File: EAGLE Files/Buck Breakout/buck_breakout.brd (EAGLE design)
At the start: 100 x 80 mm, 14 parts

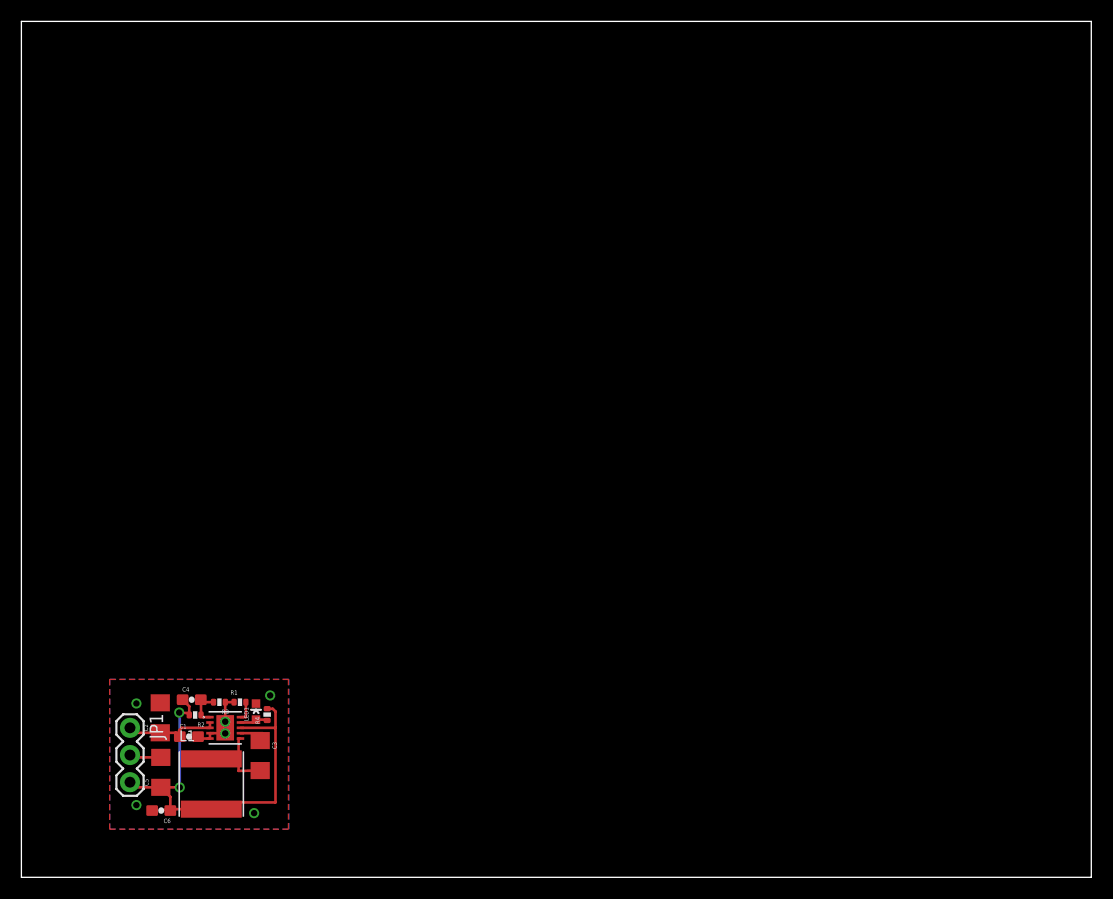
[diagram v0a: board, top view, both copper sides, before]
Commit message: Added polygons to power board. Text needs fixing.
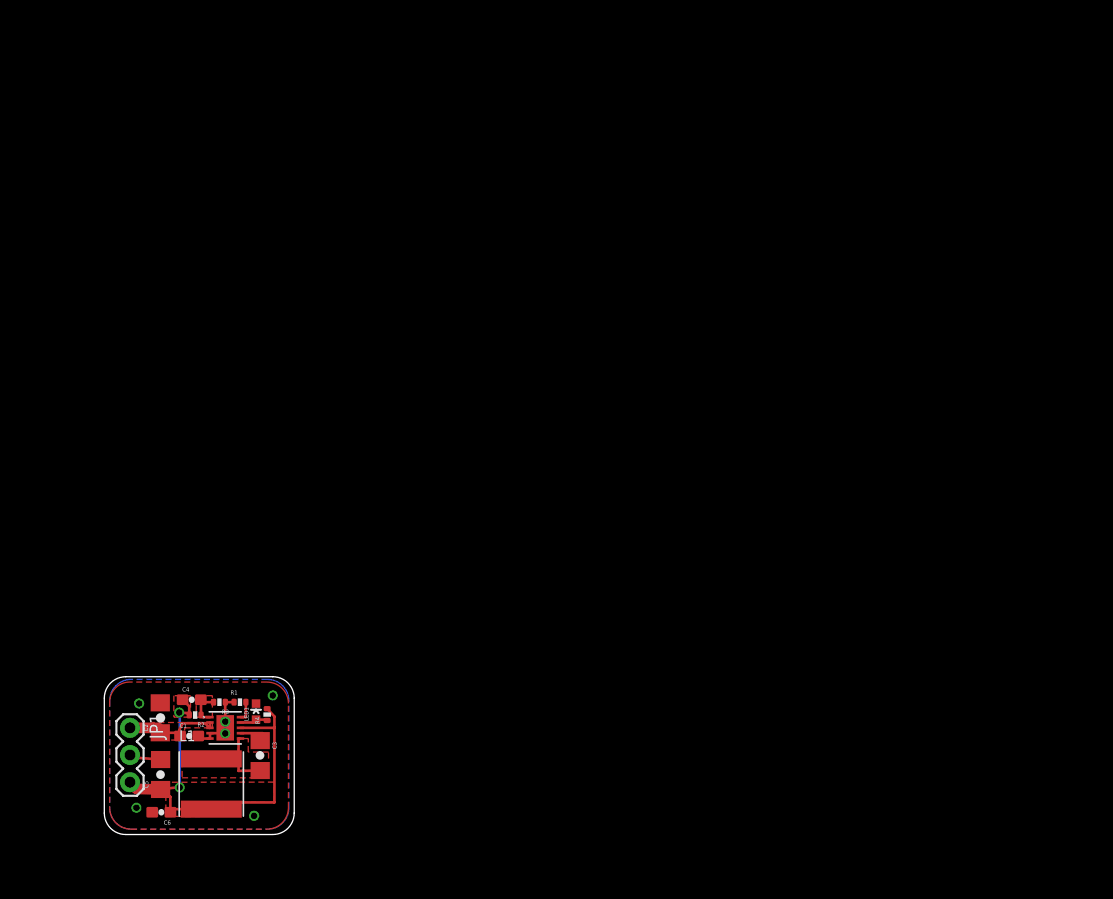
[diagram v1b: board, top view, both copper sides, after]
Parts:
- moved C5 0.20 mm to (13.0, 9.61)
- moved C6 0.16 mm to (13.1, 6.08)
- moved C1 0.06 mm to (15.7, 13.2)
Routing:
- net VOUT: track 40.9 -> 39.9 mm
- net VIN: track 9.09 -> 9.99 mm
- added copper zone on layer 1, net FB
- added copper zone on layer 1, net SW
- added copper zone on layer 1, net VIN
- added copper zone on layer 1, net VOUT
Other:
- board size 100 x 80 mm -> 17.8 x 14.8 mm

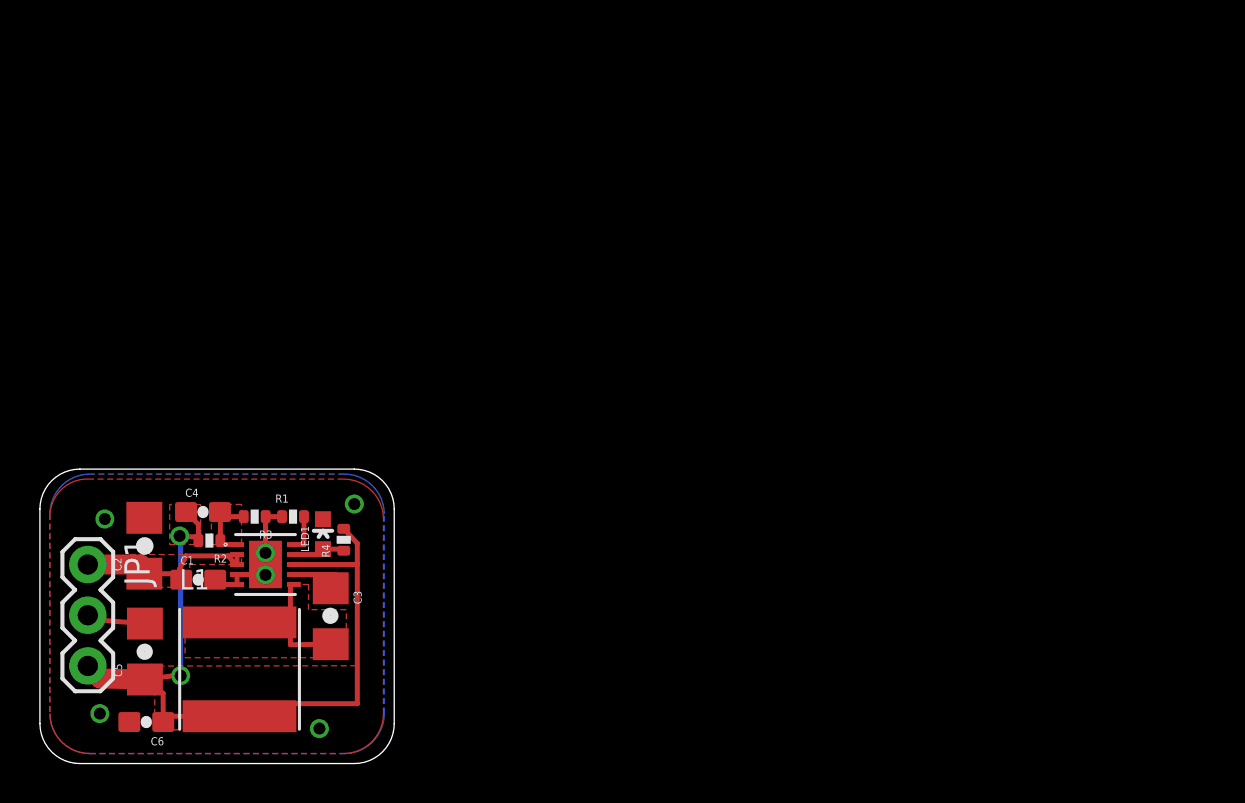
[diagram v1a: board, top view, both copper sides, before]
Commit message: Added linear reg to power board. Layout ver 1.
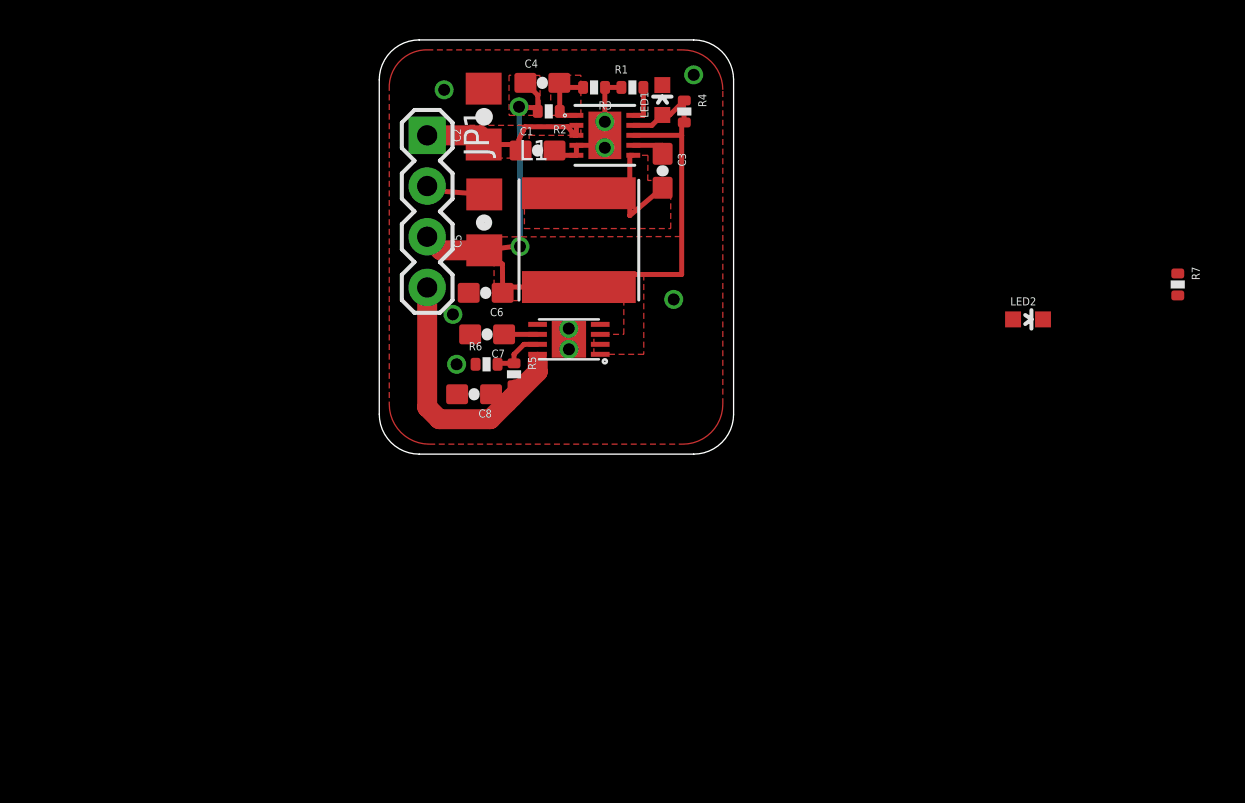
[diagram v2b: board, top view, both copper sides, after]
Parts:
- added C7: 1000pF, chips:0603-CAP
- added C8: 1uF, chips:0603-CAP
- added LED2: (no value), chips:LED-0603
- added R5, R6: 1M, chips:0402-S
- added R7: 330, chips:0402-S
- added U$2: MCP1725, intelliDesk:2X3_DFN
- C3: device chips:1206 -> chips:0603-CAP
- JP1: device SparkFun-Connectors:1X03 -> SparkFun-Connectors:1X04
- moved C3 27.8 mm to (38.9, 33.7)
- moved LED1 27.6 mm to (38.9, 37.2)
- moved R4 27.4 mm to (40.0, 36.7), turned to 270 degrees
- moved R2 27.4 mm to (33.2, 36.7)
- moved C1 27.4 mm to (32.7, 34.7)
- moved C2 27.4 mm to (30.0, 36.4)
- moved C4 27.4 mm to (32.9, 38.1)
- moved C5 27.4 mm to (30.0, 31.1)
- moved C6 27.4 mm to (30.1, 27.6)
- moved JP1 27.4 mm to (27.1, 35.5)
- moved L1 27.4 mm to (34.8, 30.2)
- moved R1 27.4 mm to (37.4, 37.9)
- moved U$1 27.4 mm to (36.0, 35.5)
- moved R3 27.4 mm to (35.5, 37.9)
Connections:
- removed net VOUT: C4.1, C5.1, C6.1, JP1.3, L1.2, R2.2, R4.2, U$1.8
- new net 3.3V: C8.1, JP1.4, R5.2, R7.1, U$2.8
- new net 3.6V: C4.1, C5.1, C6.1, JP1.3, L1.2, R2.2, R4.2, U$1.8, U$2.1, U$2.2, U$2.3
- new net N$1: LED2.A, R7.2, U$2.5
- new net N$5: C7.1, U$2.6
- new net N$6: R5.1, R6.2, U$2.7
- net GND: now also C7.2, C8.2, LED2.C, R6.1, U$2.4, U$2.EP
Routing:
- net VOUT: track 39.9 -> 0.00 mm, vias 2 -> 0
- net 3.6V: track 0.00 -> 37.3 mm, vias 0 -> 2
- net 3.3V: track 0.00 -> 15.3 mm
- net N$6: track 0.00 -> 2.68 mm
- net N$5: track 0.00 -> 1.68 mm
- net N$4: track 2.82 -> 1.90 mm
- net GND: vias 6 -> 9
- added copper zone on layer 1, net 3.6V
- removed copper zone on layer 16, net GND
- removed copper zone on layer 1, net VOUT
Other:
- board size 17.8 x 14.8 mm -> 17.8 x 20.8 mm

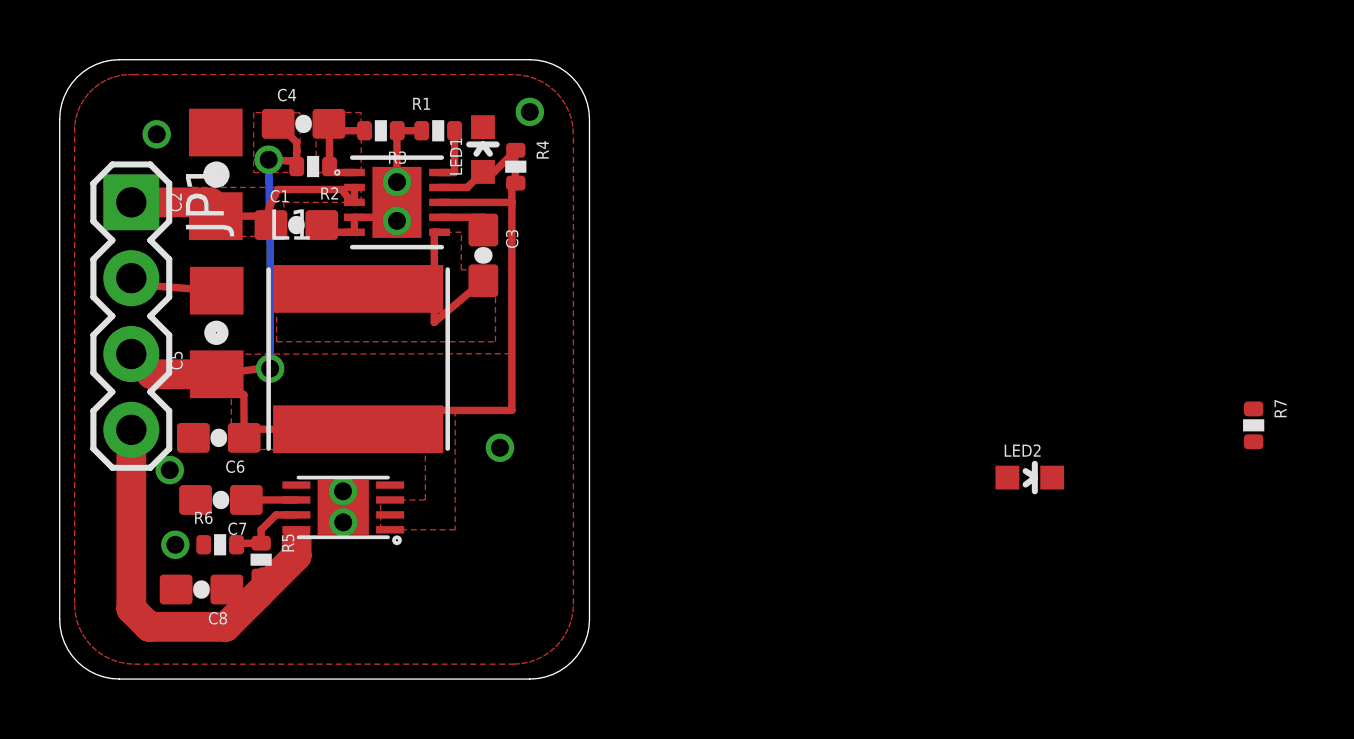
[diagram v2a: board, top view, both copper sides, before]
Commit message: Rerouted for nicer layout on linear supply
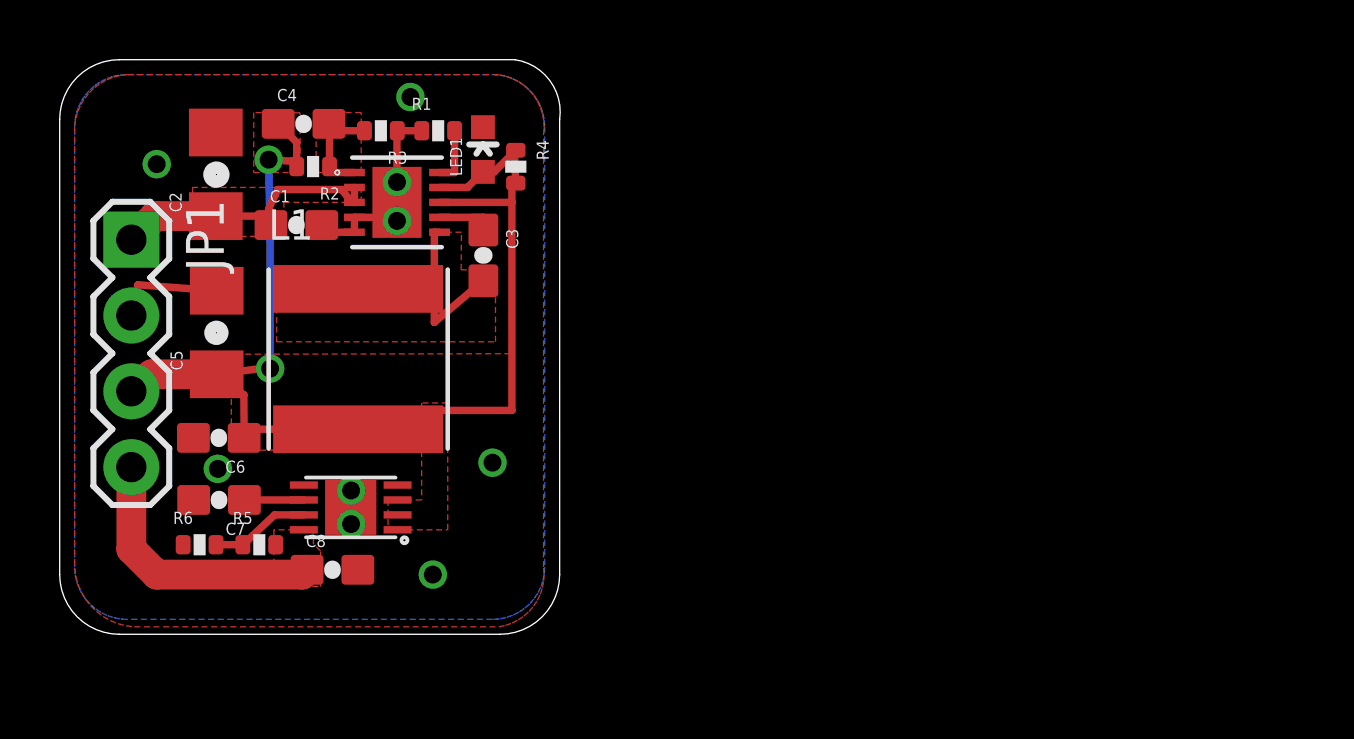
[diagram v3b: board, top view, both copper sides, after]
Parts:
- removed LED2: (no value), chips:LED-0603
- removed R7: 330, chips:0402-S
- moved C8 4.44 mm to (33.9, 23.2), turned to 0 degrees
- moved JP1 1.25 mm to (27.1, 34.2)
- moved R6 0.69 mm to (29.4, 24.0)
- moved R5 0.50 mm to (31.4, 24.0), turned to 0 degrees
- moved U$2 0.25 mm to (34.5, 25.2)
- moved C7 0.06 mm to (30.1, 25.5)
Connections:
- removed net N$1: LED2.A, R7.2, U$2.5
- net 3.3V: no longer R7.1
- net GND: no longer LED2.C
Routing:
- net 3.3V: track 15.3 -> 9.06 mm
- net GND: track 9.96 -> 10.7 mm
- net N$6: track 2.68 -> 3.34 mm
- added copper zone on layer 1, net 3.3V
- added copper zone on layer 16, net GND
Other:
- board size 17.8 x 20.8 mm -> 16.8 x 19.2 mm

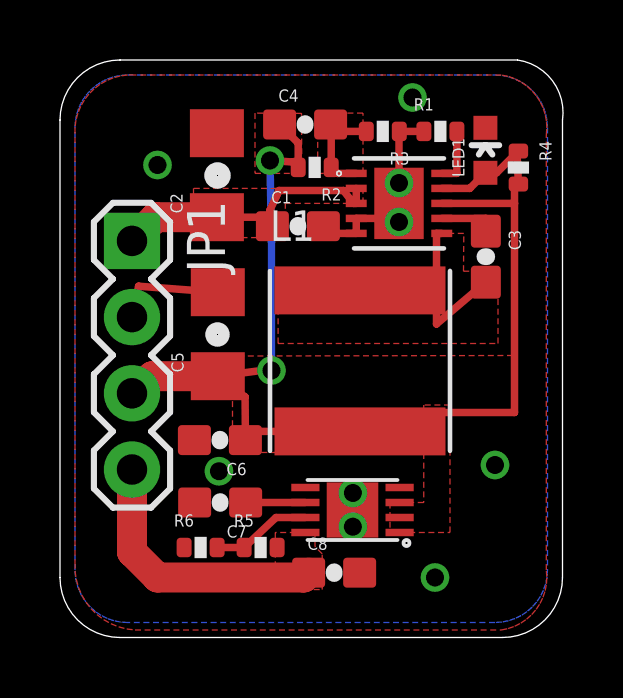
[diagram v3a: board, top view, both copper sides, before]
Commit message: fixed via size and removed most silkscreen on power breakout pcb
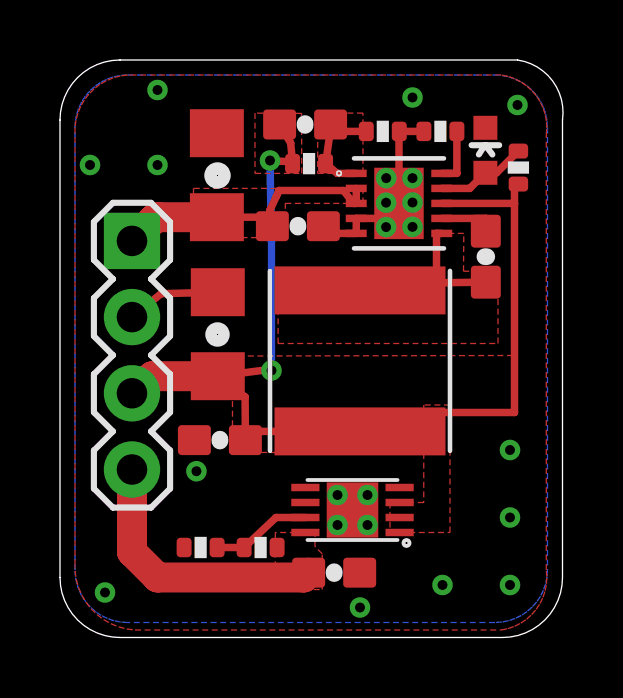
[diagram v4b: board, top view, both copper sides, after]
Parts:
- removed C7: 1000pF, chips:0603-CAP
- moved R2 0.23 mm to (33.1, 36.8)
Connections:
- removed net N$5: C7.1, U$2.6
- net GND: no longer C7.2
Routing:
- net N$5: track 1.99 -> 0.00 mm
- net SW: track 8.17 -> 6.41 mm
- net 3.6V: track 37.2 -> 35.6 mm
- net GND: track 10.7 -> 10.1 mm, vias 9 -> 22

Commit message: Removed unneeded capacitor on linear supply. Turns out that cap was needed only for power good indicator.
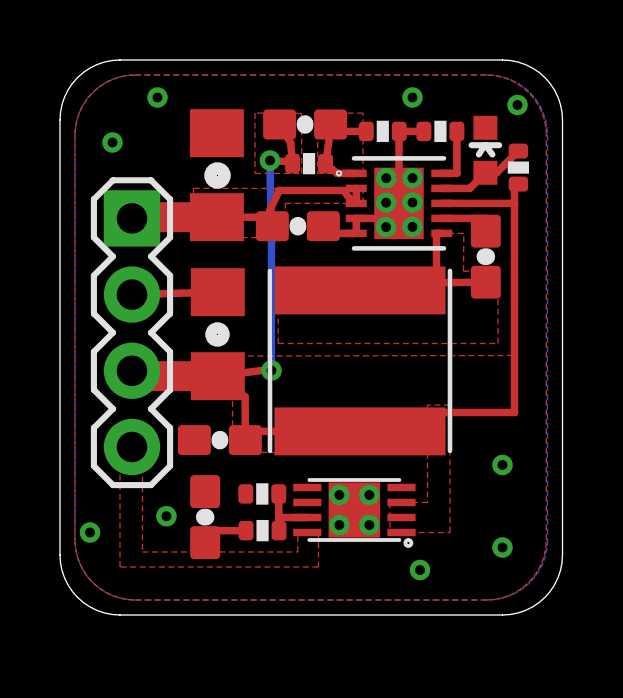
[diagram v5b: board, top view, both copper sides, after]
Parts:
- moved C8 4.68 mm to (29.6, 25.0), turned to 90 degrees
- moved R6 2.72 mm to (31.5, 25.8)
- moved JP1 0.75 mm to (27.1, 35.0)
- moved R5 0.57 mm to (31.5, 24.6), turned to 180 degrees
- moved U$2 0.06 mm to (34.6, 25.2)
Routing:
- net 3.3V: track 9.06 -> 1.76 mm
- net N$6: track 3.34 -> 2.17 mm
- net GND: track 10.1 -> 9.86 mm, vias 22 -> 19
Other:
- board size 16.8 x 19.2 mm -> 16.8 x 18.5 mm

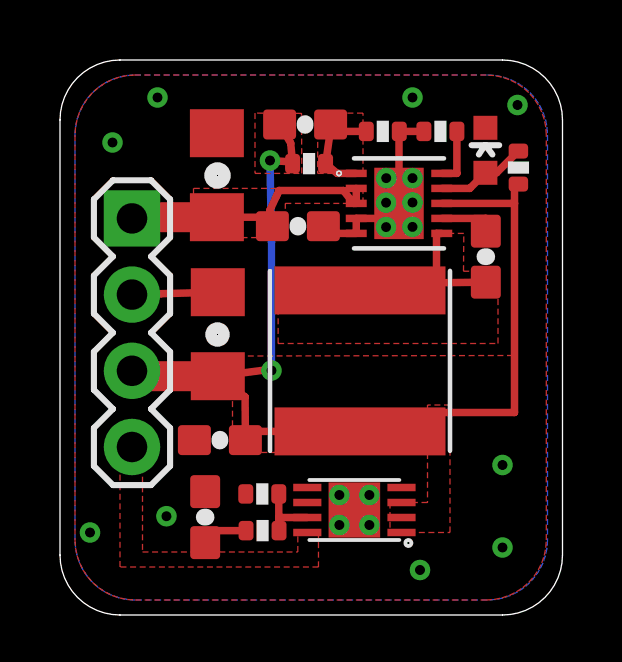
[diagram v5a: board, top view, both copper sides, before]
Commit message: Added OLED breakout board. (not yet designed) Added linear regulator datasheet. Updated parts library.
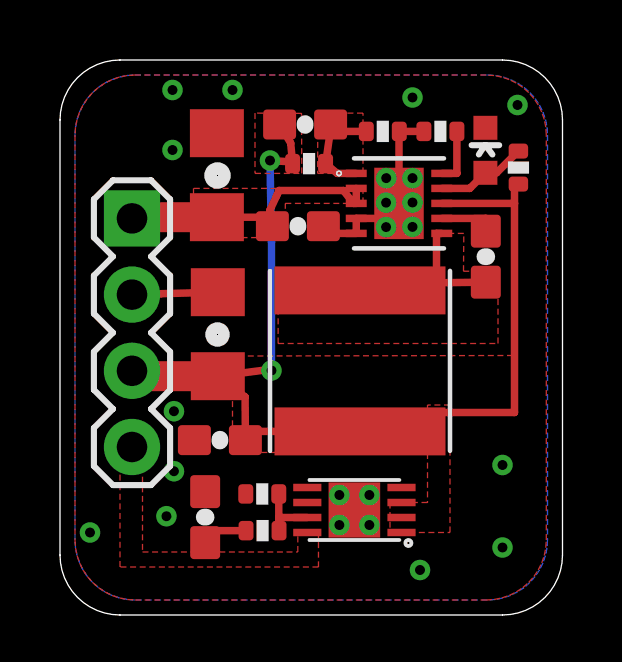
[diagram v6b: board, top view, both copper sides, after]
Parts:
- R5: value 1M -> 1.1M
- R6: value 1M -> 160k
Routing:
- net GND: vias 19 -> 22
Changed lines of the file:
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@@
 </element>
 <element name="U$2" library="intelliDesk" package="2X3_DFN" value="MCP1725" x="34.5626" y="25.25" smashed="yes" rot="R180"/>
-<element name="R5" library="chips" package="0402-S" value="1M" x="31.5016" y="24.5622" smashed="yes" rot="R180"/>
-<element name="R6" library="chips" package="0402-S" value="1M" x="31.4926" y="25.7852" smashed="yes"/>
+<element name="R5" library="chips" package="0402-S" value="1.1M" x="31.5016" y="24.5622" smashed="yes" rot="R180"/>
+<element name="R6" library="chips" package="0402-S" value="160k" x="31.4926" y="25.7852" smashed="yes"/>
 <element name="C8" library="chips" package="0603-CAP" value="1uF" x="29.5886" y="25.0124" smashed="yes" rot="R90"/>
 </elements>
@@
 <via x="36.5" y="35.5" extent="1-16" drill="0.3302"/>
 <via x="36.5" y="34.6874" extent="1-16" drill="0.3302"/>
-<via x="26.5" y="37.5" extent="1-16" drill="0.3302"/>
-<via x="28" y="39" extent="1-16" drill="0.3302"/>
+<via x="28.5" y="39.25" extent="1-16" drill="0.3302"/>
+<via x="30.5" y="39.25" extent="1-16" drill="0.3302"/>
 <via x="40" y="38.75" extent="1-16" drill="0.3302"/>
 <via x="39.5" y="26.75" extent="1-16" drill="0.3302"/>
@@
 <via x="39.5" y="24" extent="1-16" drill="0.3302"/>
 <via x="25.75" y="24.5" extent="1-16" drill="0.3302"/>
+<via x="28.548" y="26.5424" extent="1-16" drill="0.3302"/>
+<via x="28.548" y="28.5424" extent="1-16" drill="0.3302"/>
+<via x="28.5" y="37.25" extent="1-16" drill="0.3302"/>
 </signal>
 <signal name="N$4">
